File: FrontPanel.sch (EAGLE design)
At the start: 24 parts, among them U1 TPIC6B595N, U2 TPIC6B595N, U3 TPIC6B595N, U4 TPIC6B595N, U5 TPIC6B595N, U6 TPIC6B595N

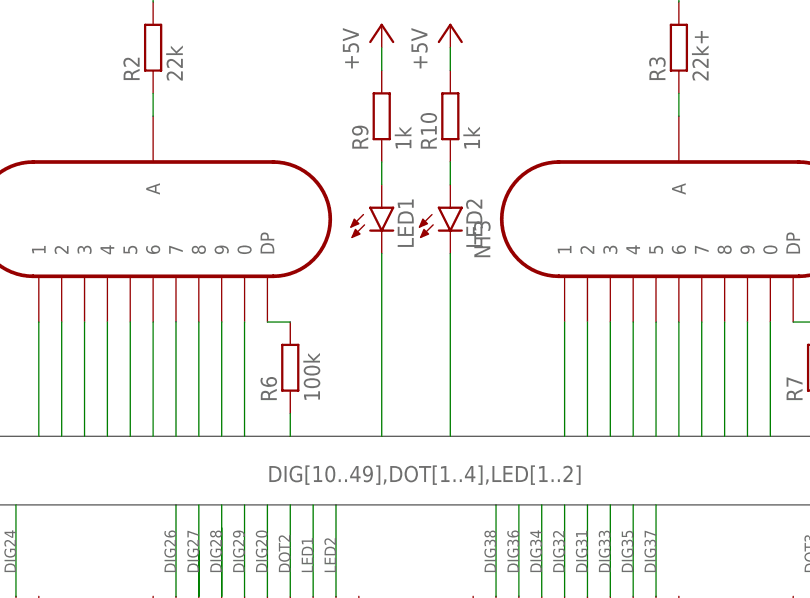
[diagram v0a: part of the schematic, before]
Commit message: switched to smd LEDs and added Light-Pipes
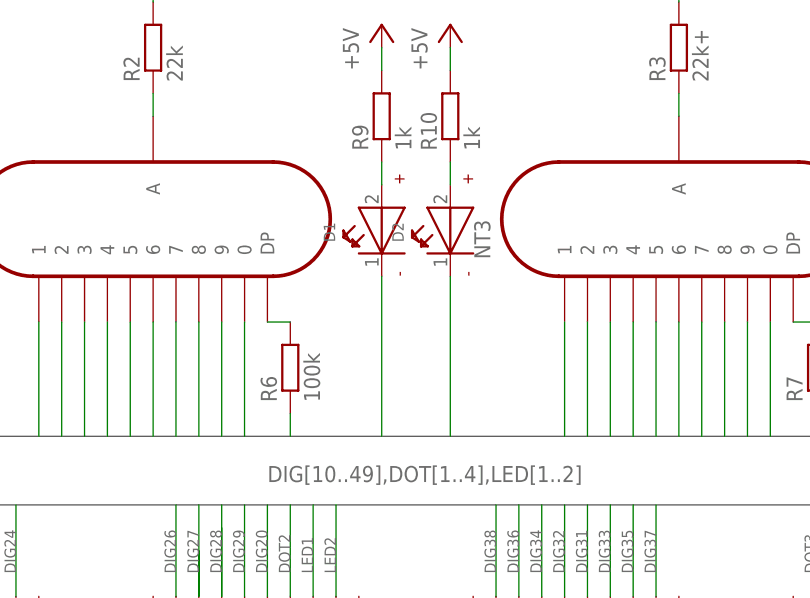
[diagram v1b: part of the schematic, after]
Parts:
- removed LED1, LED2: (no value), led:LED5MM
- added D1, D2: (no value), Wurth_Elektronik_Optoelectronics_rev17b:WL-SMTW_3528-150141AS73100-A
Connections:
- net LED1: now also D1.-; no longer LED1.C
- net LED2: now also D2.-; no longer LED2.C
- net N$66: now also D1.+; no longer LED1.A
- net N$67: now also D2.+; no longer LED2.A
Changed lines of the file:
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@@
 <part name="P+6" library="supply1" library_urn="urn:adsk.eagle:library:371" deviceset="+5V" device=""/>
 <part name="P+10" library="supply1" library_urn="urn:adsk.eagle:library:371" deviceset="+5V" device=""/>
-<part name="LED1" library="led" library_urn="urn:adsk.eagle:library:259" deviceset="LED" device="5MM" package3d_urn="urn:adsk.eagle:package:15799/2"/>
-<part name="LED2" library="led" library_urn="urn:adsk.eagle:library:259" deviceset="LED" device="5MM" package3d_urn="urn:adsk.eagle:package:15799/2"/>
 <part name="R9" library="rcl" library_urn="urn:adsk.eagle:library:334" deviceset="R-EU_" device="0207/10" package3d_urn="urn:adsk.eagle:package:23491/2" value="1k"/>
 <part name="R10" library="rcl" library_urn="urn:adsk.eagle:library:334" deviceset="R-EU_" device="0207/10" package3d_urn="urn:adsk.eagle:package:23491/2" value="1k"/>
@@
 <part name="SUPPLY15" library="supply2" library_urn="urn:adsk.eagle:library:372" deviceset="+UB" device="" value="+160V"/>
 <part name="DATA" library="pinhead" library_urn="urn:adsk.eagle:library:325" deviceset="PINHD-1X5" device="" package3d_urn="urn:adsk.eagle:package:22469/2"/>
+<part name="D1" library="Wurth_Elektronik_Optoelectronics_rev17b" library_urn="urn:adsk.eagle:library:446" deviceset="WL-SMTW_3528" device="-150141AS73100-A" package3d_urn="urn:adsk.eagle:package:32264/1"/>
+<part name="D2" library="Wurth_Elektronik_Optoelectronics_rev17b" library_urn="urn:adsk.eagle:library:446" deviceset="WL-SMTW_3528" device="-150141AS73100-A" package3d_urn="urn:adsk.eagle:package:32264/1"/>
 </parts>
 <sheets>
@@
 <attribute name="VALUE" x="7.62" y="-2.54" size="1.778" layer="96" rot="R90"/>
 </instance>
-<instance part="LED1" gate="G$1" x="104.14" y="88.9" smashed="yes">
-<attribute name="NAME" x="107.696" y="84.328" size="1.778" layer="95" rot="R90"/>
-<attribute name="VALUE" x="109.855" y="84.328" size="1.778" layer="96" rot="R90"/>
-</instance>
-<instance part="LED2" gate="G$1" x="111.76" y="88.9" smashed="yes">
-<attribute name="NAME" x="115.316" y="84.328" size="1.778" layer="95" rot="R90"/>
-<attribute name="VALUE" x="117.475" y="84.328" size="1.778" layer="96" rot="R90"/>
-</instance>
 <instance part="R9" gate="G$1" x="104.14" y="99.06" smashed="yes" rot="R90">
 <attribute name="NAME" x="102.6414" y="95.25" size="1.778" layer="95" rot="R90"/>
@@
 <attribute name="NAME" x="39.37" y="-33.655" size="1.778" layer="95" rot="R180"/>
 <attribute name="VALUE" x="39.37" y="-15.24" size="1.778" layer="96" rot="R180"/>
+</instance>
+<instance part="D1" gate="G$1" x="104.14" y="86.36" smashed="yes" rot="R90">
+<attribute name="NAME" x="98.968" y="85.072" size="1.27" layer="95" rot="R90"/>
+<attribute name="VALUE" x="109.668" y="85.132" size="1.27" layer="96" rot="R90"/>
+</instance>
+<instance part="D2" gate="G$1" x="111.76" y="86.36" smashed="yes" rot="R90">
+<attribute name="NAME" x="106.588" y="85.072" size="1.27" layer="95" rot="R90"/>
+<attribute name="VALUE" x="117.288" y="85.132" size="1.27" layer="96" rot="R90"/>
 </instance>
 </instances>
@@
 <net name="LED1" class="0">
 <segment>
-<pinref part="LED1" gate="G$1" pin="C"/>
-<wire x1="104.14" y1="63.5" x2="104.14" y2="83.82" width="0.1524" layer="91"/>
+<wire x1="104.14" y1="63.5" x2="104.14" y2="81.28" width="0.1524" layer="91"/>
+<pinref part="D1" gate="G$1" pin="-"/>
 </segment>
 <segment>
@@
 <net name="LED2" class="0">
 <segment>
-<pinref part="LED2" gate="G$1" pin="C"/>
-<wire x1="111.76" y1="63.5" x2="111.76" y2="83.82" width="0.1524" layer="91"/>
+<wire x1="111.76" y1="63.5" x2="111.76" y2="81.28" width="0.1524" layer="91"/>
+<pinref part="D2" gate="G$1" pin="-"/>
 </segment>
 <segment>
@@
 <segment>
 <pinref part="R9" gate="G$1" pin="1"/>
-<pinref part="LED1" gate="G$1" pin="A"/>
-<wire x1="104.14" y1="93.98" x2="104.14" y2="91.44" width="0.1524" layer="91"/>
+<pinref part="D1" gate="G$1" pin="+"/>
+<wire x1="104.14" y1="91.44" x2="104.14" y2="93.98" width="0.1524" layer="91"/>
 </segment>
 </net>
@@
 <segment>
 <pinref part="R10" gate="G$1" pin="1"/>
-<pinref part="LED2" gate="G$1" pin="A"/>
 <wire x1="111.76" y1="93.98" x2="111.76" y2="91.44" width="0.1524" layer="91"/>
-</segment>
-</net>
+<pinref part="D2" gate="G$1" pin="+"/>
+</segment>
+</net>
